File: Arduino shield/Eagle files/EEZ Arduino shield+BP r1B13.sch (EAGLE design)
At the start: 181 parts, among them IC1 TLC5925, IC10 SN74LV125APW, IC11 SI8620EC-B-IS, IC12 SI8620EC-B-IS, IC13 Si8660EC-B-IS1, IC14 PCA21125, IC15 AT25256B, IC16 ENC28J60-I/SS, IC17 BC857BS, IC18 NE555D, IC19 BC857BS, IC2 SN74LVCC3245ADBRSSOP, IC20 NE555D, IC21 SN74LV1T34, IC3 SN74LVCC3245ADBRSSOP, IC4 SN74LVCC3245ADBRSSOP, IC5 SN74LVCC3245ADBRSSOP, IC6 LD1117ADT33TR, IC7 SN74LVCC3245ADBRSSOP, IC8 SN74LVCC3245ADBRSSOP, IC9 Si8660EC-B-IS1, J1 BS-244DSM-R, J2 BS-244DSM-B, J3 BS-244DSM-R, J4 BS-244DSM-G, J5 BS-244DSM-B, Q1 IRLML2246TRPBF, Q10 2N7002, Q11 2N7002, Q12 2N7002, Q13 2N7002, Q2 IRLML2246TRPBF, Q3 IRLML2246TRPBF, Q4 2N7002, Q5 IRLML2246TRPBF, Q6 2N7002, Q7 2N7002, Q8 2N7002, Q9 IRLML2246TRPBF, SW1 1301.9316, X1 282836-4, X10 LMJTAB881243M-L, X11 22-23-2031, X12 22-23-2031, X2 MC000005, X3 282836-4, X4 MC000005, X5 22-23-2021, X6 22-23-2041, X7 09185106324, X8 09185106324, X9 22-23-2021, Y1 32,768kHz, Y2 25MHz

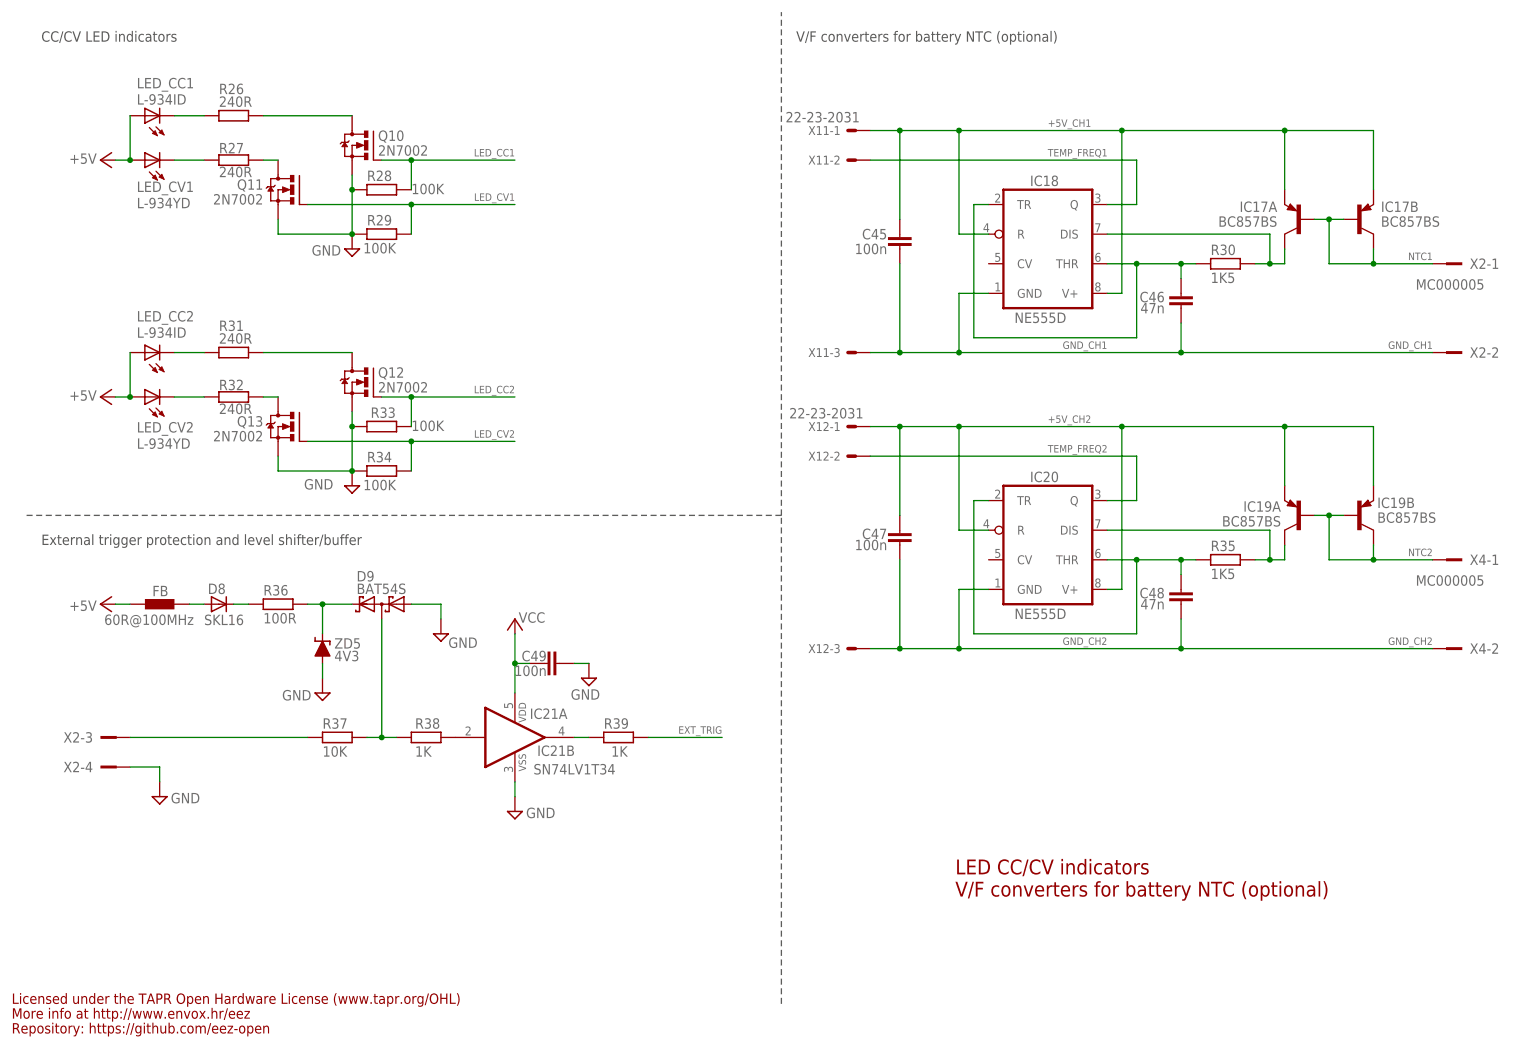
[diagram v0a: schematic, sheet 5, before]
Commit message: Arduino Shield r1B13 BOM updated
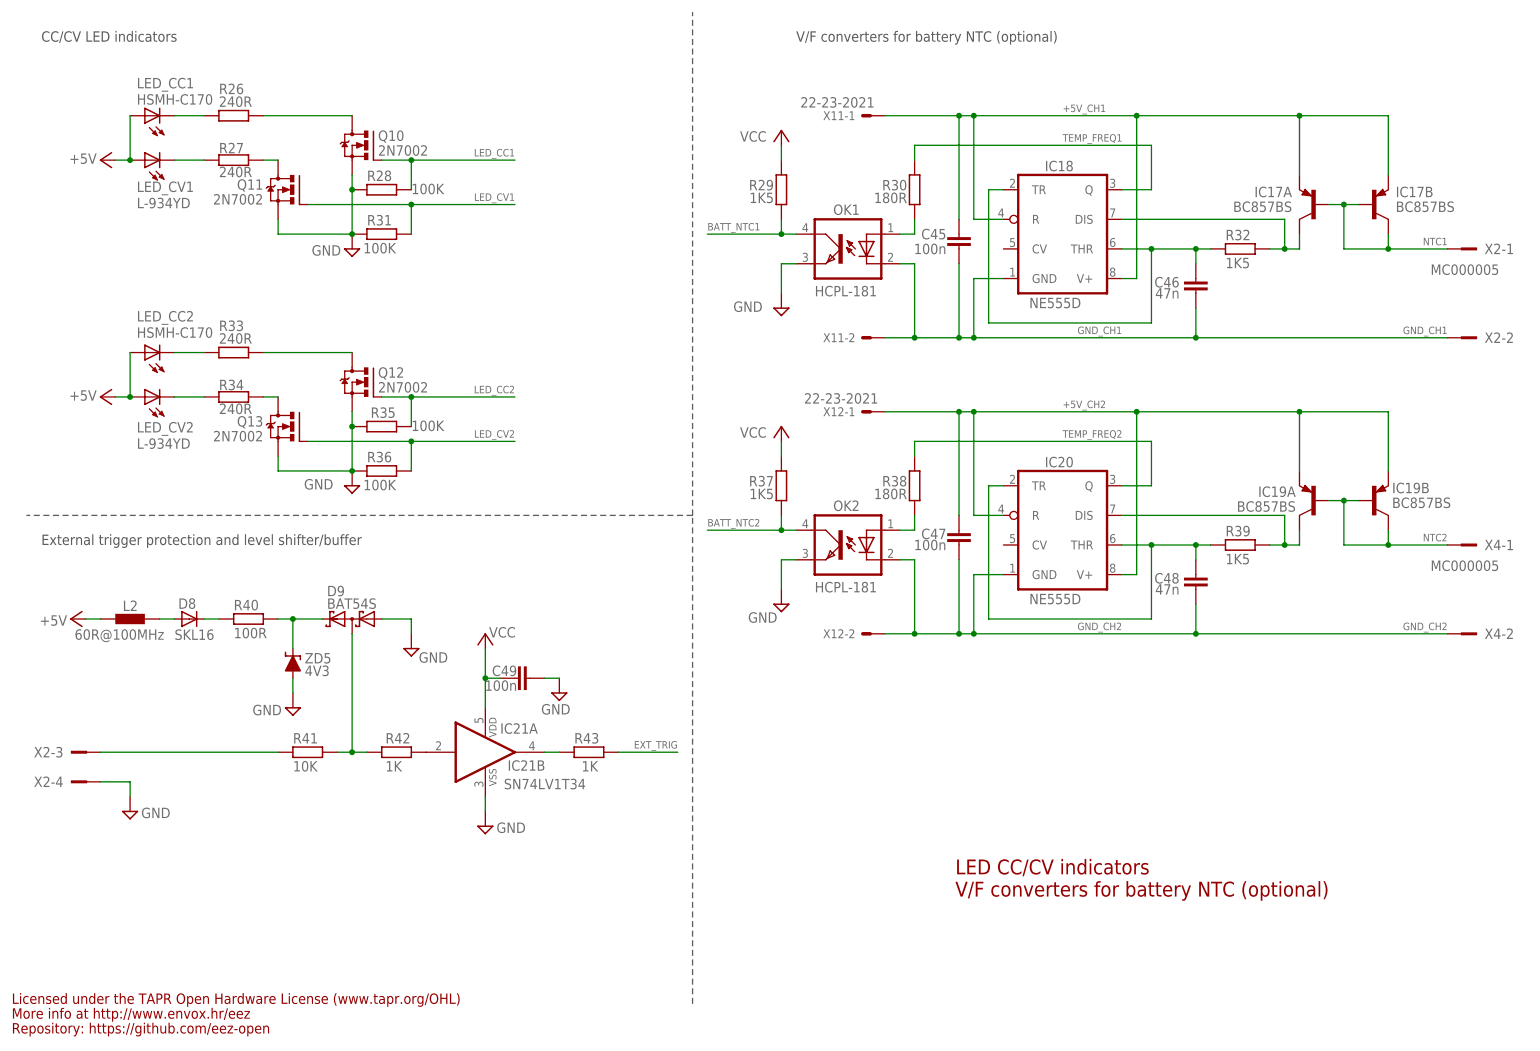
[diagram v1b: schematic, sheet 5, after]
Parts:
- removed FB: 60R@100MHz, EEZ_Lib1:FERRITE_BEAD0603
- added L2: 60R@100MHz, EEZ_Lib1:FERRITE_BEAD0603
- added OK1, OK2: HCPL-181, EEZ_Lib1:HCPL-181
- added R40: 100R, rcl:R-EU_R0805
- added R41: 10K, resistor:R-EU_R1206
- added R42, R43: 1K, rcl:R-EU_R0805
- J1, J3: value BS-244DSM-R -> BS-244DSM-R
- J4: value BS-244DSM-G -> BS-244DSM-G
- J5: value BS-244DSM-B -> BS-244DSM-B
- LED_CC1, LED_CC2: value L-934ID -> HSMH-C170
- R29: value 100K -> 1K5
- R30: value 1K5 -> 180R
- R31: value 240R -> 100K
- R32: value 240R -> 1K5
- R33, R34: value 100K -> 240R
- R35: value 1K5 -> 100K
- R36: value 100R -> 100K
- R37: value 10K -> 1K5; device resistor:R-EU_R1206 -> rcl:R-EU_R0805
- R38: value 1K -> 180R
- R39: value 1K -> 1K5
- X10: device MyLib6:RJ45-TRAFO-LED -> EEZ_Lib1:RJ45-TRAFO-LED
- X11, X12: value 22-23-2031 -> 22-23-2021; device con-molex:22-23-2031 -> con-molex:22-23-2021; MPN 22-23-2031 -> 22-23-2021; OC_FARNELL 1462950 -> 1462926; OC_NEWARK 30C0862 -> 25C3832
- renumbered LED1 to LED_01_POS, LED2 to LED_01_NEG
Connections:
- removed net WATCHDOG: MCU-ADCL.ADC5
- new net BATT_NTC1: MCU-ADCL.ADC4, OK1.COL, R29.2
- new net BATT_NTC2: MCU-ADCL.ADC3, OK2.COL, R37.2
- new net N$22: OK1.A, R30.2
- new net N$36: OK2.A, R38.2
- net +5V: now also L2.1; no longer FB.1
- net EXT_TRIG: now also R43.1; no longer R39.1
- net GND: now also OK1.EMIT, OK2.EMIT, R31.2, R35.2, R36.2; no longer R29.2, R33.2, R34.2
- net GND_CH1: now also OK1.C, X11-2.S; no longer X11-3.S
- net GND_CH2: now also OK2.C, X12-2.S; no longer X12-3.S
- net LED_CC2: now also R35.1; no longer R33.1
- net LED_CV1: now also R31.1; no longer R29.1
- net LED_CV2: now also R36.1; no longer R34.1
- net N$1: now also R43.2; no longer R39.2
- net N$12: now also R33.2; no longer R31.2
- net N$14: now also R34.2; no longer R32.2
- net N$15: now also R33.1; no longer R31.1
- net N$16: now also R32.2; no longer R30.2
- net N$17: now also R39.1; no longer R35.1
- net N$18: now also R32.1; no longer R30.1
- net N$19: now also R39.2; no longer R35.2
- net N$2: now also R40.1; no longer R36.1
- net N$23: now also R34.1; no longer R32.1
- net N$26: now also R41.2, R42.2; no longer R37.2, R38.2
- net N$27: now also R42.1; no longer R38.1
- net N$3: now also L2.2; no longer FB.2
- net N$33: now also R40.2; no longer R36.2
- net N$4: now also R41.1; no longer R37.1
- net TEMP_FREQ1: now also R30.1; no longer X11-2.S
- net TEMP_FREQ2: now also R38.1; no longer X12-2.S
- net VCC: now also R29.1, R37.1
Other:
- note added: "Battery NTC"
- note removed: "Ch#1 NTC"
- moved on the sheet: C45, C46, C47, C48, C49, D8, D9, IC17A, IC17B, IC18, IC19A, IC19B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
